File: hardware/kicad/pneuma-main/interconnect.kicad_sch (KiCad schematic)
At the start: 5 parts, among them J4 CAMERA, J5 TO_PWR

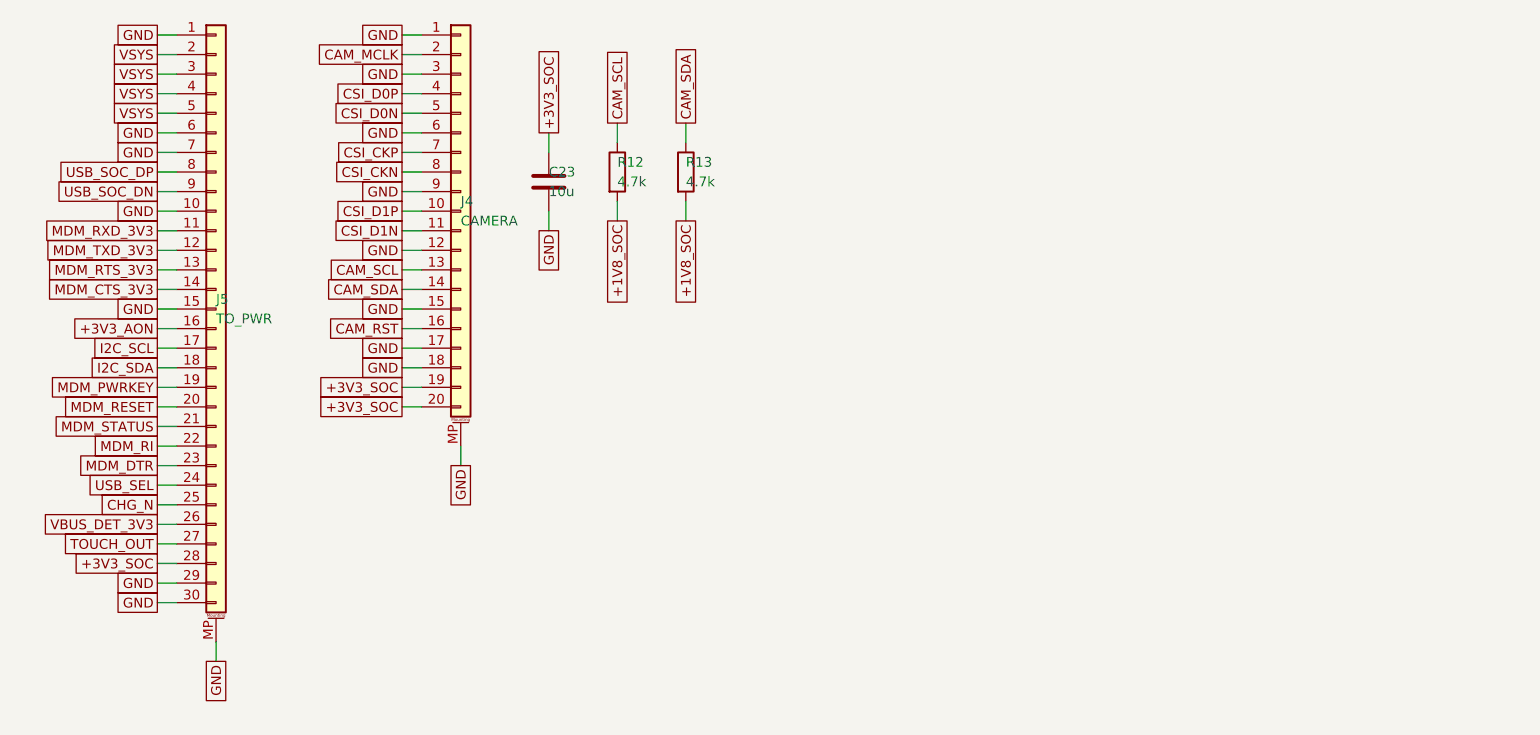
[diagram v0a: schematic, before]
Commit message: Move the touch pad under the camera bump, per the intended interaction
The touch area was over the battery, following K's "thin touch area" on the
lower front face.  It should sit ~10 mm below the camera bump, where a finger
lands: a 24 x 16 mm electrode at x -12..12, y -12..4 on the front membrane.

Consequences carried through:
- the AT42QT1011 front-end moves from PNM-PWR to PNM-MAIN beside the nRF, so
  the electrode run is short and TOUCH_OUT no longer crosses the FFC.  FFC pin
  27 becomes GND
- the electrode contacts PNM-MAIN TP11 at (11.0, 4.6)
- the speaker moves +2.2 mm in y to clear the pad.  It stays the 1 W 15 mm
  round part: the only sub-15 mm options are 5 mW earpiece receivers, and the
  15x11 alternative is 0.3 W (~5 dB quieter)
- the copper spreader keep-out follows the pad

Sensitivity is now the open question: the battery pouch is 1-2 mm behind the
pad's lower half and the speaker sits just above it.  Both are in REV-A.md as
bench-tuning items (Cs, and a foam spacer to hold the electrode off the metal).
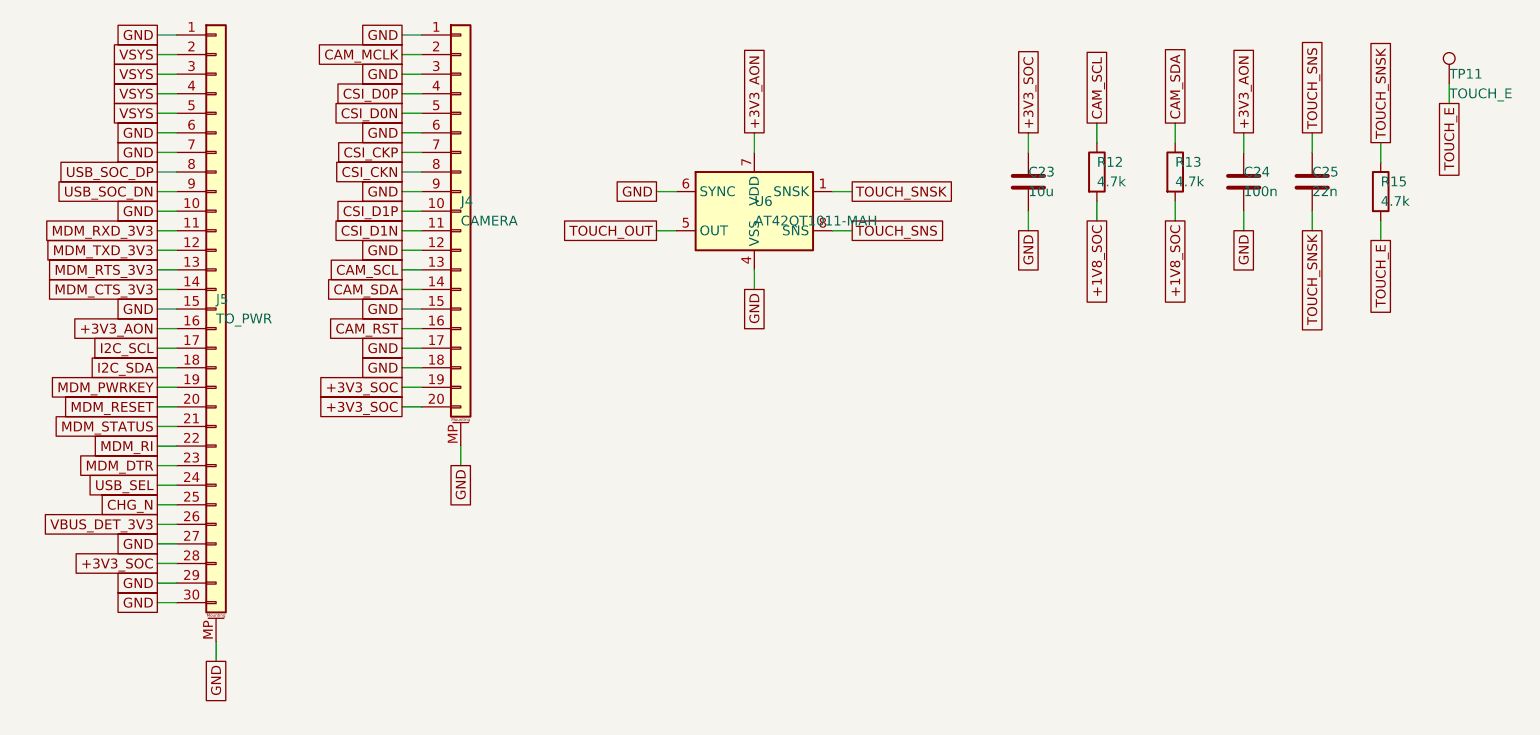
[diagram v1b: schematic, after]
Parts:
- added C24: 100n, Capacitor_SMD:C_0402_1005Metric, symbol Device:C
- added C25: 22n, Capacitor_SMD:C_0402_1005Metric, symbol Device:C
- added R15: 4.7k, Resistor_SMD:R_0402_1005Metric, symbol Device:R
- added TP11: TOUCH_E, Pneuma:SpringPad_3.0x2.0mm, symbol Connector:TestPoint
- added U6: AT42QT1011-MAH, Package_DFN_QFN:DFN-8-1EP_2x2mm_P0.5mm_EP0.9x1.5mm, symbol Sensor_Touch:AT42QT1011-M
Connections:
- net +3V3_AON: now also C24.1, U6.7 (VDD)
- net GND: now also J5.27 (Pin_27), C24.2, U6.4 (VSS), U6.6 (SYNC), U6.9 (VSS)
- net TOUCH_OUT: now also U6.5 (OUT); no longer J5.27 (Pin_27)
- new net TOUCH_E: R15.2, TP11.1
- new net TOUCH_SNS: C25.1, U6.8 (SNS)
- new net TOUCH_SNSK: C25.2, R15.1, U6.1 (SNSK)
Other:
- moved on the sheet: C23, R12, R13
